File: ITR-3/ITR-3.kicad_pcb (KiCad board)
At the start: 2 copper layers, 15 parts

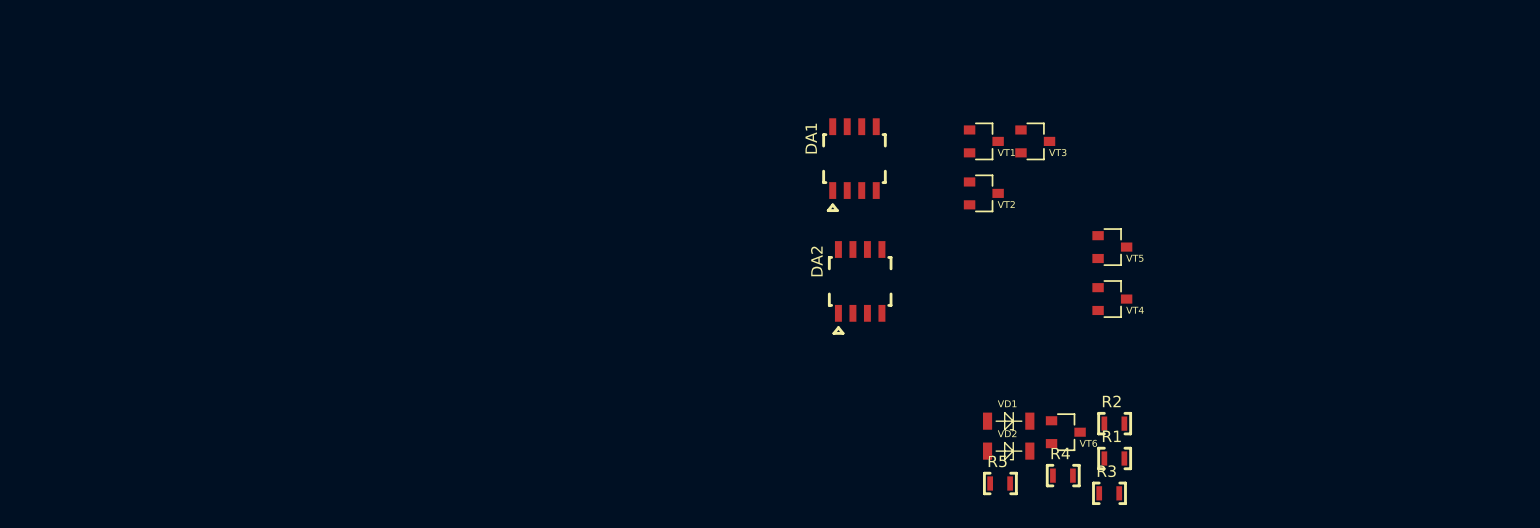
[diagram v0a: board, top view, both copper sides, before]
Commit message: обновлена схема - добавлен буферный входной ОУ
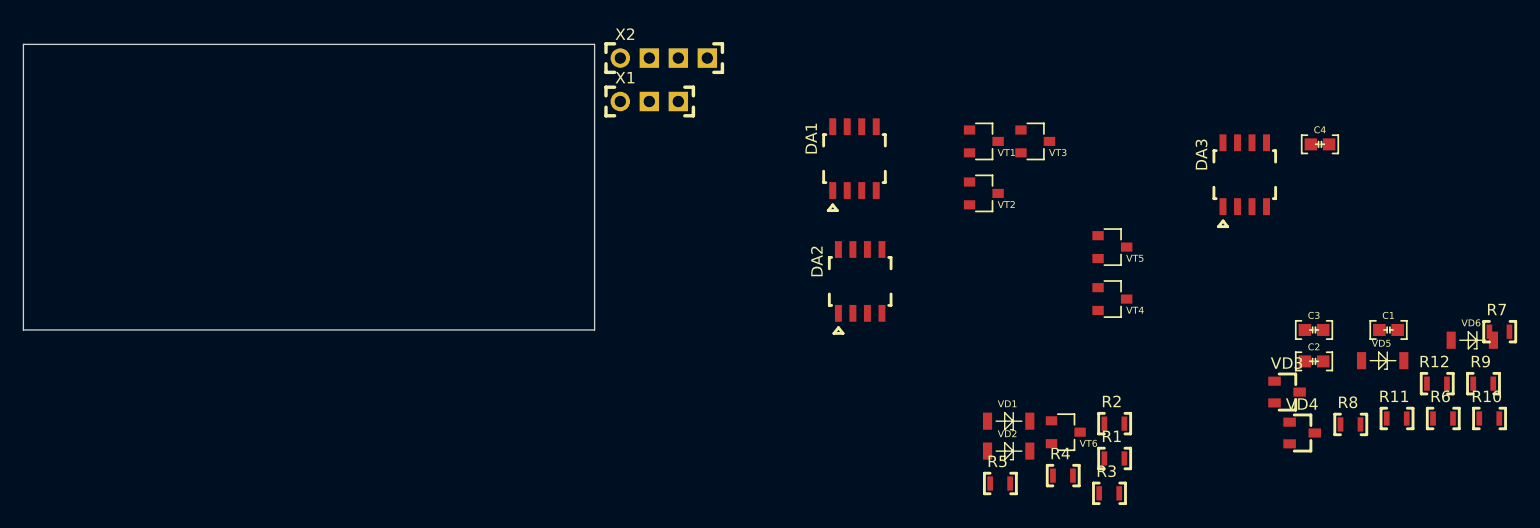
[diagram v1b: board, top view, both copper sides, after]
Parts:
- added C1: Конденсатор*0,1мкФ*25В*0603, N_RLC:Конденсатор_SMD_IEC_0603, F.Cu at (169.5, 100.0)
- added C2: Конденсатор*0,1мкФ*25В*0603, N_RLC:Конденсатор_SMD_IEC_0603, F.Cu at (163.0, 102.8)
- added C3: Конденсатор*0,1мкФ*25В*0603, N_RLC:Конденсатор_SMD_IEC_0603, F.Cu at (163.0, 100.0)
- added C4: Конденсатор*0,1мкФ*25В*0603, N_RLC:Конденсатор_SMD_IEC_0603, F.Cu at (163.5, 83.8)
- added DA3: ОУ_LMx58, N_DD:SO-8, F.Cu at (156.9, 86.4)
- added R10: Резистор_0,065Вт, N_RLC:Резистор_SMD_0603_0,065_Вт, F.Cu at (178.3, 107.8)
- added R11: Резистор_0,065Вт, N_RLC:Резистор_SMD_0603_0,065_Вт, F.Cu at (170.2, 107.8)
- added R12: Резистор_0,065Вт, N_RLC:Резистор_SMD_0603_0,065_Вт, F.Cu at (173.7, 104.7)
- added R6: Резистор_0,065Вт, N_RLC:Резистор_SMD_0603_0,065_Вт, F.Cu at (174.3, 107.8)
- added R7: Резистор_0,065Вт, N_RLC:Резистор_SMD_0603_0,065_Вт, F.Cu at (179.2, 100.2)
- added R8: Резистор_0,065Вт, N_RLC:Резистор_SMD_0603_0,065_Вт, F.Cu at (166.2, 108.3)
- added R9: Резистор_0,065Вт, N_RLC:Резистор_SMD_0603_0,065_Вт, F.Cu at (177.8, 104.7)
- added VD3: Диоды_шоттки_BAT54S, N_VD_HL:Транзистор_IRLML6344TR_SOT-23, F.Cu at (160.6, 105.4)
- added VD4: Диоды_шоттки_BAT54S, N_VD_HL:Транзистор_IRLML6344TR_SOT-23, F.Cu at (161.9, 109.0)
- added VD5: Стабилитрон_1N5352BRLG_вертикальный, N_VD_HL:SOD-80, F.Cu at (167.1, 102.7)
- added VD6: Стабилитрон_1N5352BRLG_вертикальный, N_VD_HL:SOD-80, F.Cu at (175.0, 100.9)
- added X1: Вилка_PLS3, N_X:Вилка_PLS3_вертикальная, F.Cu at (102.2, 80.0)
- added X2: Вилка_PLS4, N_X:Вилка_PLS4_вертикальная, F.Cu at (102.2, 76.2)
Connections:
- DA1 pad 1: unconnected-(DA1-Pad1) -> /DA-A
- DA1 pad 2: unconnected-(DA1-Pad2) -> /TX-OUT
- DA1 pad 3: unconnected-(DA1-Pad3) -> AREF
- DA1 pad 4: unconnected-(DA1-Pad4) -> GND
- DA1 pad 5: unconnected-(DA1-Pad5) -> /TX-OUT
- DA1 pad 6: unconnected-(DA1-Pad6) -> AREF
- DA1 pad 7: unconnected-(DA1-Pad7) -> /DA-B
- DA1 pad 8: unconnected-(DA1-Pad8) -> 5V
- DA2 pad 4: unconnected-(DA2-Pad4) -> GND
- DA2 pad 8: unconnected-(DA2-Pad8) -> 5V
- R1 pad 2: /TXB -> /DA-A
- R2 pad 2: /TXB -> /DA-A
- R4 pad 1: /TXA -> GND
- R4 pad 2: Net-(R4-Pad2) -> /RSEN
- R5 pad 1: /TXA -> Net-(VT2-Pad3)
- R5 pad 2: Net-(R5-Pad2) -> Net-(VT3-Pad2)
- VD2 pad 1: Net-(R4-Pad2) -> Net-(R7-Pad2)
- VT1 pad 1: unconnected-(VT1-Pad1) -> /RSEN
- VT1 pad 3: Net-(R3-Pad1) -> Net-(VT1-Pad3)
- VT3 pad 2: Net-(VT2-Pad3) -> Net-(VT3-Pad2)
- VT5 pad 2: Net-(VT2-Pad3) -> Net-(VT3-Pad2)
- VT6 pad 1: Net-(R5-Pad2) -> Net-(R8-Pad2)
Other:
- board outline added: 50 x 25 mm

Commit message: подготовлена трассировка и GBR для заказа
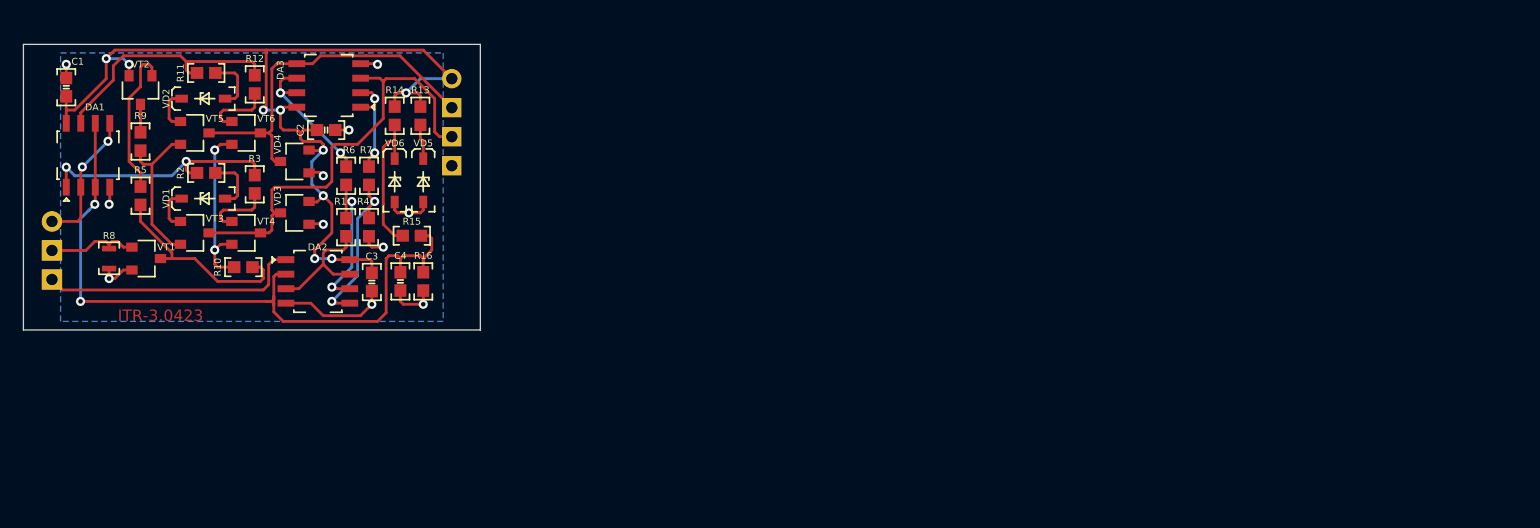
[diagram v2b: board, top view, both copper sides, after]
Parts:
- removed the C4 at (163.5, 83.8)
- removed the R8 at (166.2, 108.3)
- removed the X1 at (102.2, 80.0)
- added C3: Конденсатор*0,1мкФ*25В*0603, KICAD6_RLC:Конденсатор_SMD_IEC_0603, F.Cu at (80.5, 95.8)
- added R13: smd-резистор*4,7*0,1Вт*5проц*0603*ВП, KICAD6_RLC:Резистор_SMD_IEC_0603-0,1_Вт, F.Cu at (84.8, 81.2)
- added R14: smd-резистор*1к*0,1Вт*5проц*0603*ВП, KICAD6_RLC:Резистор_SMD_IEC_0603-0,1_Вт, F.Cu at (82.5, 81.2)
- added R15: smd-резистор*10к*0,1Вт*5проц*0603*ВП, KICAD6_RLC:Резистор_SMD_IEC_0603-0,1_Вт, F.Cu at (84.0, 91.8)
- added R16: smd-резистор*10к*0,1Вт*5проц*0603*ВП, KICAD6_RLC:Резистор_SMD_IEC_0603-0,1_Вт, F.Cu at (85.0, 95.8)
- added R4: smd-резистор*100к*0603*ВП, MOTOR_RLC:Резистор_SMD_IEC_0603-0,075_Вт, F.Cu at (80.2, 91.0)
- added XP1: Вилка*PLS*3контакта*1ряд*вертикальная, MOTOR_X:Вилка_SNP346-3VP21-1, B.Cu at (52.5, 90.5)
- C1, C2: footprint N_RLC:Конденсатор_SMD_IEC_0603 -> KICAD6_RLC:Конденсатор_SMD_IEC_0603
- C4: renamed from C3; footprint N_RLC:Конденсатор_SMD_IEC_0603 -> KICAD6_RLC:Конденсатор_SMD_IEC_0603
- DA1, DA2, DA3: value ОУ_LMx58 -> ОУ*сдвоенный*so-8*ОТК; footprint N_DD:SO-8 -> MOTOR_IMPORT_OTK:SO-8
- R1: value Резистор_0,065Вт -> smd-резистор*100к*0603*ВП; footprint N_RLC:Резистор_SMD_0603_0,065_Вт -> MOTOR_RLC:Резистор_SMD_IEC_0603-0,075_Вт
- R10, R9: value Резистор_0,065Вт -> smd-резистор*4,7*0,1Вт*5проц*0603*ВП; footprint N_RLC:Резистор_SMD_0603_0,065_Вт -> KICAD6_RLC:Резистор_SMD_IEC_0603-0,1_Вт
- R11, R2: value Резистор_0,065Вт -> smd-резистор*470*0,1Вт*5проц*0603*ВП; footprint N_RLC:Резистор_SMD_0603_0,065_Вт -> KICAD6_RLC:Резистор_SMD_IEC_0603-0,1_Вт
- R12, R3, R5: value Резистор_0,065Вт -> smd-резистор*1к*0,1Вт*5проц*0603*ВП; footprint N_RLC:Резистор_SMD_0603_0,065_Вт -> KICAD6_RLC:Резистор_SMD_IEC_0603-0,1_Вт
- R6, R7: value Резистор_0,065Вт -> smd-резистор*20к*0603*ВП; footprint N_RLC:Резистор_SMD_0603_0,065_Вт -> MOTOR_RLC:Резистор_SMD_IEC_0603-0,075_Вт
- VD1, VD2, VD5, VD6: value Стабилитрон_1N5352BRLG_вертикальный -> smd-стабилитрон*5,1В*5мА*КД-36*ВП; footprint N_VD_HL:SOD-80 -> MOTOR_VD_VT_HL:Корпус_IEC_КД-36
- VD3, VD4: footprint N_VD_HL:Транзистор_IRLML6344TR_SOT-23 -> MOTOR_VD_VT_HL:Корпус_КТ-46
- X1: renamed from X2; moved to B.Cu
- moved R9 119.4 mm to (60.2, 83.5), turned to 90 degrees
- moved C1 117.7 mm to (53.8, 78.8), turned to -90 degrees
- moved R10 109.9 mm to (69.2, 94.5), turned to 180 degrees
- moved R11 108.5 mm to (66.0, 77.5), turned to 180 degrees
- moved R12 106.8 mm to (70.2, 78.5), turned to -90 degrees
- moved R7 99.9 mm to (80.2, 86.5), turned to 90 degrees
- moved R6 98.3 mm to (78.2, 86.5), turned to 90 degrees
- moved VD6 93.5 mm to (82.5, 86.9), turned to -90 degrees
- moved VD4 91.3 mm to (73.8, 85.2), turned to 180 degrees
- moved C2 88.8 mm to (76.5, 82.5), turned to 180 degrees
- moved VD3 88.3 mm to (73.8, 89.8), turned to 180 degrees
- moved R8 85.6 mm to (57.5, 93.8), turned to 90 degrees
- moved VD5 83.6 mm to (85.0, 86.9), turned to -90 degrees
- moved R2 82.5 mm to (66.0, 86.2)
- moved VT5 80.9 mm to (65.0, 82.8)
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- renumbered R4 to R8
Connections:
- C1 pad 1: 5V -> GND
- C1 pad 2: GND -> 5V
- C2 pad 1: 5V -> GND
- C2 pad 2: GND -> 5V
- C4 pad 1: AREF -> GND
- C4 pad 2: GND -> AREF
- DA2 pad 1: unconnected-(DA2-Pad1) -> /RX-IN
- DA2 pad 2: unconnected-(DA2-Pad2) -> AREF
- DA2 pad 3: unconnected-(DA2-Pad3) -> Net-(DA2-Pad3)
- DA2 pad 5: unconnected-(DA2-Pad5) -> Net-(DA2-Pad5)
- DA2 pad 6: unconnected-(DA2-Pad6) -> Net-(DA2-Pad6)
- DA2 pad 7: unconnected-(DA2-Pad7) -> Net-(DA2-Pad3)
- DA3 pad 1: unconnected-(DA3-Pad1) -> /BUFA
- DA3 pad 2: unconnected-(DA3-Pad2) -> /BUFA
- DA3 pad 3: unconnected-(DA3-Pad3) -> /RSA
- DA3 pad 5: unconnected-(DA3-Pad5) -> /RSB
- DA3 pad 6: unconnected-(DA3-Pad6) -> /BUFB
- DA3 pad 7: unconnected-(DA3-Pad7) -> /BUFB
- R1 pad 1: Net-(R1-Pad1) -> Net-(DA2-Pad3)
- R1 pad 2: /DA-A -> Net-(DA2-Pad6)
- R10 pad 1: 5V -> Net-(R10-Pad1)
- R11 pad 1: Net-(R10-Pad2) -> Net-(R11-Pad1)
- R11 pad 2: AREF -> /DA-B
- R12 pad 1: AREF -> /DA-B
- R12 pad 2: GND -> Net-(R12-Pad2)
- R2 pad 1: Net-(R2-Pad1) -> /DA-A
- R2 pad 2: /DA-A -> Net-(R2-Pad2)
- R3 pad 2: Net-(R3-Pad2) -> /DA-A
- R5 pad 1: Net-(VT2-Pad3) -> Net-(R10-Pad1)
- R5 pad 2: Net-(VT3-Pad2) -> Net-(R5-Pad2)
- R6 pad 1: Net-(R3-Pad1) -> Net-(DA2-Pad6)
- R6 pad 2: Net-(VT1-Pad3) -> /BUFB
- R7 pad 1: /DA-B -> Net-(DA2-Pad5)
- R7 pad 2: Net-(R7-Pad2) -> /BUFA
- R9 pad 1: 5V -> Net-(R9-Pad1)
- VT1 pad 3: Net-(VT1-Pad3) -> Net-(R10-Pad1)
- VT2 pad 1: Net-(R3-Pad2) -> Net-(R5-Pad2)
- VT2 pad 3: Net-(VT2-Pad3) -> Net-(R9-Pad2)
- VT3 pad 1: Net-(VD1-Pad2) -> Net-(VD1-PadK)
- VT3 pad 2: Net-(VT3-Pad2) -> Net-(R9-Pad1)
- VT4 pad 1: Net-(R2-Pad1) -> Net-(R3-Pad1)
- VT4 pad 2: Net-(R3-Pad1) -> Net-(R10-Pad2)
- VT5 pad 1: Net-(VD2-Pad2) -> Net-(VD2-PadK)
- VT5 pad 2: Net-(VT3-Pad2) -> Net-(R9-Pad1)
- VT6 pad 1: Net-(R8-Pad2) -> Net-(R12-Pad2)
- VT6 pad 2: Net-(R3-Pad1) -> Net-(R10-Pad2)
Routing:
- net 5V: track 0.00 -> 89.4 mm, vias 0 -> 9
- net AREF: track 0.00 -> 62.6 mm, vias 0 -> 2
- net /RSA: track 0.00 -> 39.3 mm
- net /RSB: track 0.00 -> 32.4 mm
- net GND: track 0.00 -> 31.5 mm, vias 0 -> 11
- net /RX-IN: track 0.00 -> 23.0 mm
- net /DA-B: track 0.00 -> 22.4 mm
- net /DA-A: track 0.00 -> 21.9 mm, vias 0 -> 2
- net Net-(R10-Pad1): track 0.00 -> 17.6 mm
- net Net-(DA2-Pad5): track 0.00 -> 15.3 mm, vias 0 -> 2
- net Net-(R10-Pad2): track 0.00 -> 15.2 mm, vias 0 -> 2
- net Net-(R9-Pad1): track 0.00 -> 13.8 mm
- net Net-(R5-Pad2): track 0.00 -> 13.2 mm
- net /BUFB: track 0.00 -> 12.8 mm, vias 0 -> 2
- net Net-(R14-Pad1): track 0.00 -> 12.8 mm
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- added copper zone on B.Cu, net GND
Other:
- board size 50 x 25 mm -> 40 x 25 mm
- board text added: "ITR-3.0423"
